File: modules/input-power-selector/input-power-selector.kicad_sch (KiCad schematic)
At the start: 33 parts, among them Q1 SI4909DY-T1-GE3, Q2 SI4909DY-T1-GE3, Q3 SI4909DY-T1-GE3, Q4 IPF067N20NM6ATMA1, Q5 BC547, Q6 SQJQ457EP, U1 LTC4417IGN

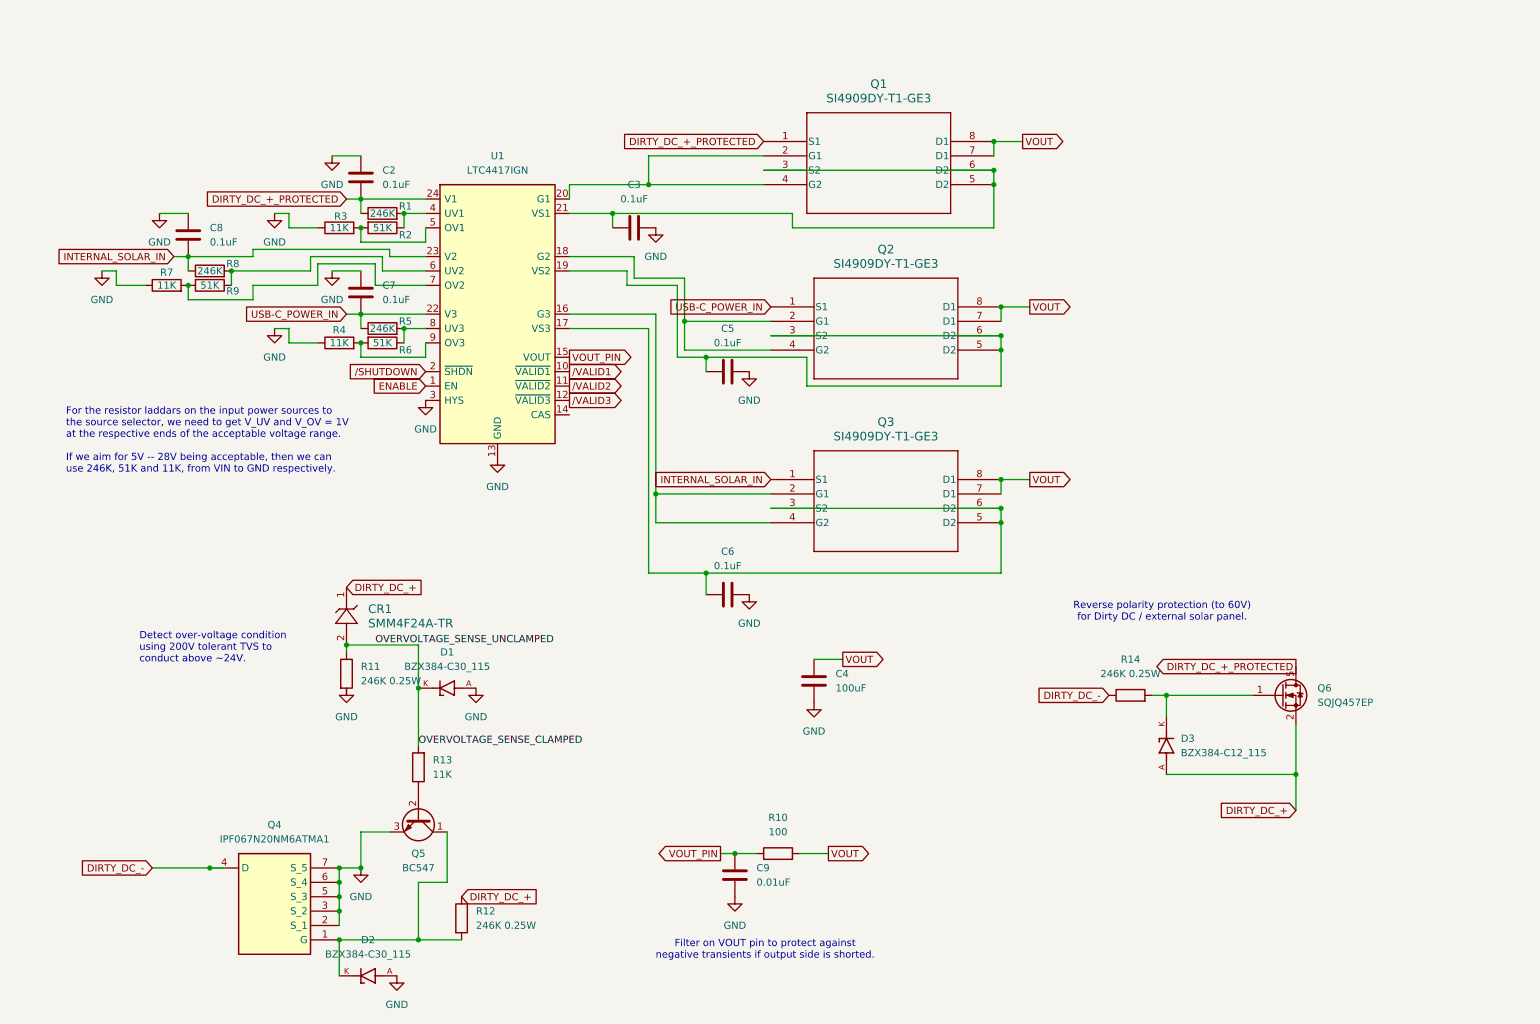
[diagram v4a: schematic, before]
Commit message: work on laying out power input selector
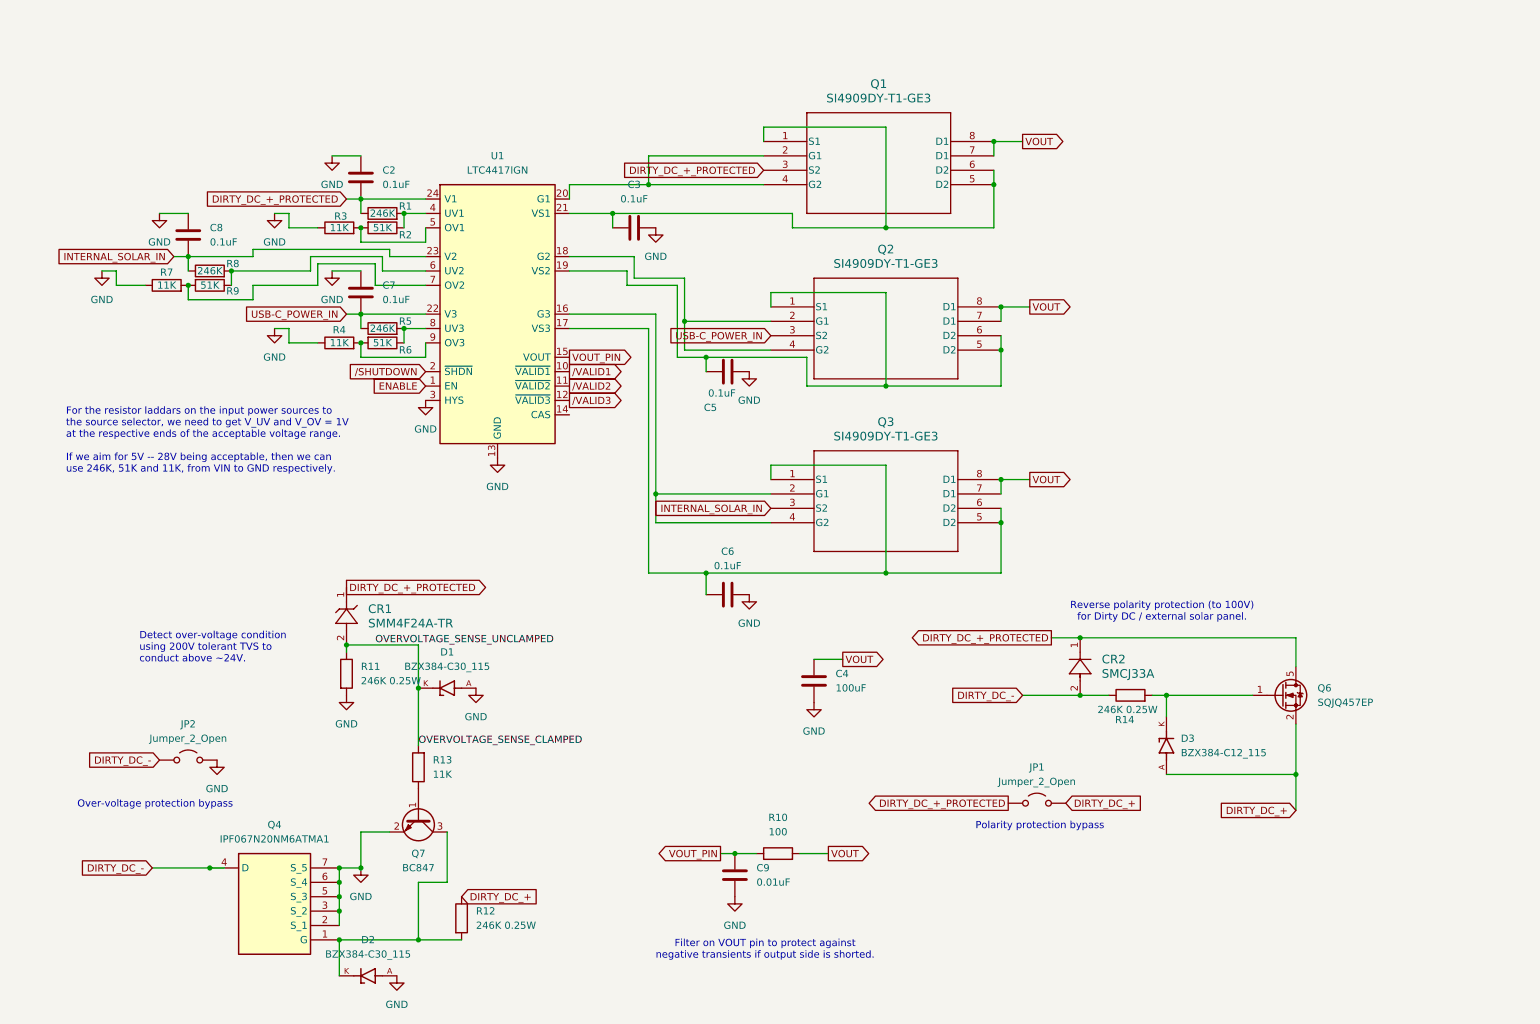
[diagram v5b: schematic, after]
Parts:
- removed Q5: BC547, Package_TO_SOT_THT:TO-92_Inline, symbol Transistor_BJT:BC547
- added CR2: SMCJ33A, DIODE_DO-214AC, symbol 2025-03-04_03-15-52:SMCJ28A
- added JP1, JP2: Jumper_2_Open, Jumper:SolderJumper-2_P1.3mm_Open_RoundedPad1.0x1.5mm, symbol Jumper:Jumper_2_Open
- added Q7: BC847, Package_TO_SOT_SMD:SOT-23, symbol Transistor_BJT:BC847
- C7: footprint (none) -> Capacitor_SMD:C_0805_2012Metric
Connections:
- net DIRTY_DC_+: now also JP1.2 (B); no longer CR1.1
- net DIRTY_DC_+_PROTECTED: now also CR1.1, Q1.3 (S2), CR2.1, JP1.1 (A); no longer Q1.1 (S1)
- net DIRTY_DC_-: now also CR2.2, JP2.1 (A)
- net GND: now also R11.2, JP2.2 (B), Q7.2 (E)
- net INTERNAL_SOLAR_IN: now also Q3.3 (S2); no longer Q3.1 (S1)
- net USB-C_POWER_IN: now also Q2.3 (S2); no longer Q2.1 (S1)
- net at D2.K, Q4.1 (G), R12.2: now also Q7.3 (C)
- net at C6.1, Q3.5 (D2), Q3.6 (D2)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: now also Q3.1 (S1); no longer Q3.3 (S2)
- net at R13.1: now also Q7.1 (B)
- net at C3.1, Q1.5 (D2), Q1.6 (D2)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: now also Q1.1 (S1); no longer Q1.3 (S2)
- net at C5.1, Q2.5 (D2), Q2.6 (D2)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: now also Q2.1 (S1); no longer Q2.3 (S2)
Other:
- note added: "Over-voltage protection bypass"
- note added: "Polarity protection bypass"
- note added: "Reverse polarity protection (to 100V) for Dirty DC / external solar panel."
- note removed: "Reverse polarity protection (to 60V) for Dirty DC / external solar panel."

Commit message: more layout fixing on power selector
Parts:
- D1, D2, D3: footprint BZX384-C30_115:DIO_BZX384-C30_115 -> footprints:DIO_BZX384-C30_115
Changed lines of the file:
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@@
 			)
 		)
-		(property "Footprint" "BZX384-C30_115:DIO_BZX384-C30_115"
+		(property "Footprint" "footprints:DIO_BZX384-C30_115"
 			(at 71.12 189.23 0)
 			(effects
@@
 			)
 		)
-		(property "Footprint" "BZX384-C30_115:DIO_BZX384-C30_115"
+		(property "Footprint" "footprints:DIO_BZX384-C30_115"
 			(at 85.09 138.43 0)
 			(effects
@@
 			)
 		)
-		(property "Footprint" "BZX384-C30_115:DIO_BZX384-C30_115"
+		(property "Footprint" "footprints:DIO_BZX384-C30_115"
 			(at 212.09 148.59 0)
 			(effects

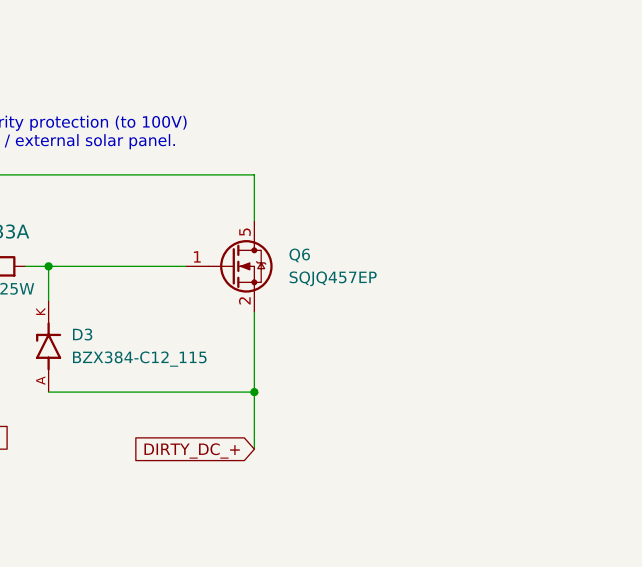
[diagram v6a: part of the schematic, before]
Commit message: update input source selecter PCB layout
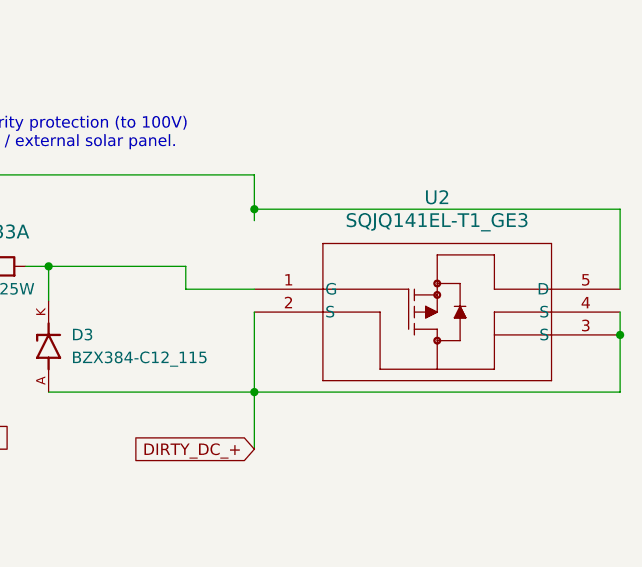
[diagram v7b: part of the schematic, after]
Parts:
- removed Q6: SQJQ457EP, Package_SO:PowerPAK_SO-8L_Single, symbol Transistor_FET:SQJQ466E
- added U2: SQJQ141EL-T1_GE3, PowerPAK_8x8L_BWL-2_VIS, symbol 2025-03-04_11-28-00:SQJQ141EL-T1_GE3
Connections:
- net DIRTY_DC_+: now also U2.2 (S), U2.3 (S), U2.4 (S)
- net DIRTY_DC_+_PROTECTED: now also U2.5 (D)
- net at D3.K, R14.2: now also U2.1 (G)
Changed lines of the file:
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@@
 	)
 	(junction
+		(at 234.95 133.35)
+		(diameter 0)
+		(color 0 0 0 0)
+	)
+	(junction
 		(at 196.85 129.54)
 		(diameter 0)
@@
 	)
 	(junction
+		(at 275.59 147.32)
+		(diameter 0)
+		(color 0 0 0 0)
+	)
+	(junction
 		(at 162.56 118.11)
 		(diameter 0)
@@
 	(wire
 		(pts
-			(xy 234.95 134.62) (xy 234.95 129.54)
+			(xy 39.37 62.23) (xy 39.37 64.77)
 		)
 		(stroke
@@
 	(wire
 		(pts
-			(xy 39.37 62.23) (xy 39.37 64.77)
+			(xy 73.66 62.23) (xy 73.66 64.77)
 		)
 		(stroke
@@
 	(wire
 		(pts
-			(xy 73.66 62.23) (xy 73.66 64.77)
+			(xy 39.37 62.23) (xy 50.8 62.23)
 		)
 		(stroke
@@
 	(wire
 		(pts
-			(xy 39.37 62.23) (xy 50.8 62.23)
+			(xy 130.81 80.01) (xy 130.81 82.55)
 		)
 		(stroke
@@
 	(wire
 		(pts
-			(xy 130.81 80.01) (xy 130.81 82.55)
+			(xy 125.73 67.31) (xy 125.73 80.01)
 		)
 		(stroke
@@
 	(wire
 		(pts
-			(xy 125.73 67.31) (xy 125.73 80.01)
+			(xy 106.68 49.53) (xy 120.65 49.53)
 		)
 		(stroke
@@
 	(wire
 		(pts
-			(xy 106.68 49.53) (xy 120.65 49.53)
+			(xy 80.01 138.43) (xy 80.01 130.81)
 		)
 		(stroke
@@
 	(wire
 		(pts
-			(xy 80.01 138.43) (xy 80.01 130.81)
+			(xy 234.95 129.54) (xy 234.95 133.35)
 		)
 		(stroke
@@
 	(wire
 		(pts
+			(xy 275.59 147.32) (xy 275.59 153.67)
+		)
+		(stroke
+			(width 0)
+			(type default)
+		)
+	)
+	(wire
+		(pts
 			(xy 72.39 63.5) (xy 62.23 63.5)
 		)
@@
 	(wire
 		(pts
+			(xy 234.95 133.35) (xy 234.95 134.62)
+		)
+		(stroke
+			(width 0)
+			(type default)
+		)
+	)
+	(wire
+		(pts
 			(xy 69.85 59.69) (xy 69.85 57.15)
 		)
@@
 	(wire
 		(pts
+			(xy 234.95 142.24) (xy 227.33 142.24)
+		)
+		(stroke
+			(width 0)
+			(type default)
+		)
+	)
+	(wire
+		(pts
 			(xy 120.65 49.53) (xy 140.97 49.53)
 		)
@@
 	(wire
 		(pts
+			(xy 275.59 144.78) (xy 275.59 147.32)
+		)
+		(stroke
+			(width 0)
+			(type default)
+		)
+	)
+	(wire
+		(pts
 			(xy 182.88 101.6) (xy 187.96 101.6)
 		)
@@
 	(wire
 		(pts
+			(xy 234.95 133.35) (xy 275.59 133.35)
+		)
+		(stroke
+			(width 0)
+			(type default)
+		)
+	)
+	(wire
+		(pts
 			(xy 118.11 66.04) (xy 127 66.04)
 		)
@@
 	(wire
 		(pts
+			(xy 227.33 142.24) (xy 227.33 139.7)
+		)
+		(stroke
+			(width 0)
+			(type default)
+		)
+	)
+	(wire
+		(pts
 			(xy 120.65 74.93) (xy 120.65 118.11)
 		)
@@
 	(wire
 		(pts
+			(xy 275.59 153.67) (xy 234.95 153.67)
+		)
+		(stroke
+			(width 0)
+			(type default)
+		)
+	)
+	(wire
+		(pts
 			(xy 182.88 109.22) (xy 182.88 118.11)
 		)
@@
 	(wire
 		(pts
+			(xy 275.59 133.35) (xy 275.59 142.24)
+		)
+		(stroke
+			(width 0)
+			(type default)
+		)
+	)
+	(wire
+		(pts
 			(xy 181.61 41.91) (xy 181.61 44.45)
 		)
@@
 	)
 	(symbol
+		(lib_id "2025-03-04_11-28-00:SQJQ141EL-T1_GE3")
+		(at 234.95 142.24 0)
+		(unit 1)
+		(exclude_from_sim no)
+		(in_bom yes)
+		(on_board yes)
+		(dnp no)
+		(fields_autoplaced yes)
+		(property "Reference" "U2"
+			(at 255.27 132.08 0)
+			(effects
+				(font
+					(size 1.524 1.524)
+				)
+			)
+		)
+		(property "Value" "SQJQ141EL-T1_GE3"
+			(at 255.27 134.62 0)
+			(effects
+				(font
+					(size 1.524 1.524)
+				)
+			)
+		)
+		(property "Footprint" "PowerPAK_8x8L_BWL-2_VIS"
+			(at 234.95 142.24 0)
+			(effects
+				(font
+					(size 1.27 1.27)
+					(italic yes)
+				)
+				(hide yes)
+			)
+		)
+		(property "Datasheet" "SQJQ141EL-T1_GE3"
+			(at 234.95 142.24 0)
+			(effects
+				(font
+					(size 1.27 1.27)
+					(italic yes)
+				)
+				(hide yes)
+			)
+		)
+		(property "Description" ""
+			(at 234.95 142.24 0)
+			(effects
+				(font
+					(size 1.27 1.27)
+				)
+				(hide yes)
+			)
+		)
+		(pin "2"
+		)
+		(pin "5"
+		)
+		(pin "4"
+		)
+		(pin "3"
+		)
+		(pin "1"
+		)
+		(instances
+			(project ""
+				(path "/c18eebf3-c622-42ce-a76a-45e5fabab2b4"
+					(reference "U2")
+					(unit 1)
+				)
+			)
+		)
+	)
+	(symbol
 		(lib_id "Device:R")
 		(at 73.66 57.15 270)
@@
 					(unit 1)
 				)
-			)
-		)
-	)
-	(symbol
-		(lib_id "Transistor_FET:SQJQ466E")
-		(at 232.41 139.7 0)
-		(unit 1)
-		(exclude_from_sim no)
-		(in_bom yes)
-		(on_board yes)
-		(dnp no)
-		(fields_autoplaced yes)
-		(property "Reference" "Q6"
-			(at 238.76 138.4299 0)
-			(effects
-				(font
-					(size 1.27 1.27)
-				)
-				(justify left)
-			)
-		)
-		(property "Value" "SQJQ457EP"
-			(at 238.76 140.9699 0)
-			(effects
-				(font
-					(size 1.27 1.27)
-				)
-				(justify left)
-			)
-		)
-		(property "Footprint" "Package_SO:PowerPAK_SO-8L_Single"
-			(at 237.49 143.51 0)
-			(effects
-				(font
-					(size 1.27 1.27)
-				)
-				(justify left)
-				(hide yes)
-			)
-		)
-		(property "Datasheet" "https://www.vishay.com/docs/75138/sqjq466e.pdf"
-			(at 237.49 146.05 0)
-			(effects
-				(font
-					(size 1.27 1.27)
-				)
-				(justify left)
-				(hide yes)
-			)
-		)
-		(property "Description" "200A Id, 60V Vds, N-Channel TrenchFET MOSFET, 1.9mOhm Ron, 14nC Qqd, -55 to 175 °C, LFPAK88"
-			(at 232.41 139.7 0)
-			(effects
-				(font
-					(size 1.27 1.27)
-				)
-				(hide yes)
-			)
-		)
-		(pin "1"
-		)
-		(pin "5"
-		)
-		(pin "4"
-		)
-		(pin "3"
-		)
-		(pin "2"
-		)
-		(instances
-			(project ""
-				(path "/c18eebf3-c622-42ce-a76a-45e5fabab2b4"
-					(reference "Q6")
-					(unit 1)
-				)

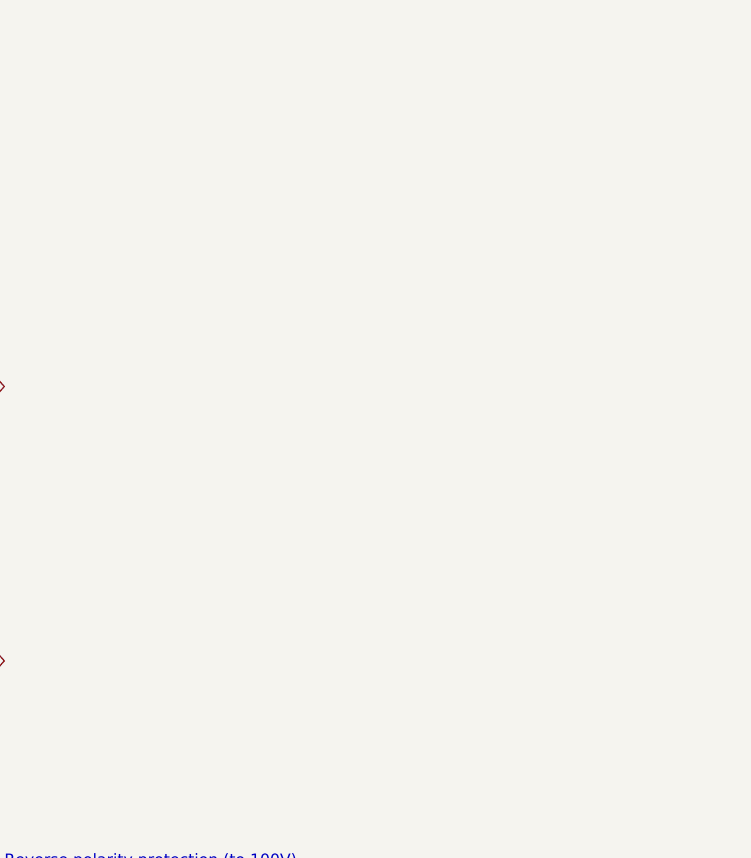
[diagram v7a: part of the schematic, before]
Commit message: add module outline for input source selecter
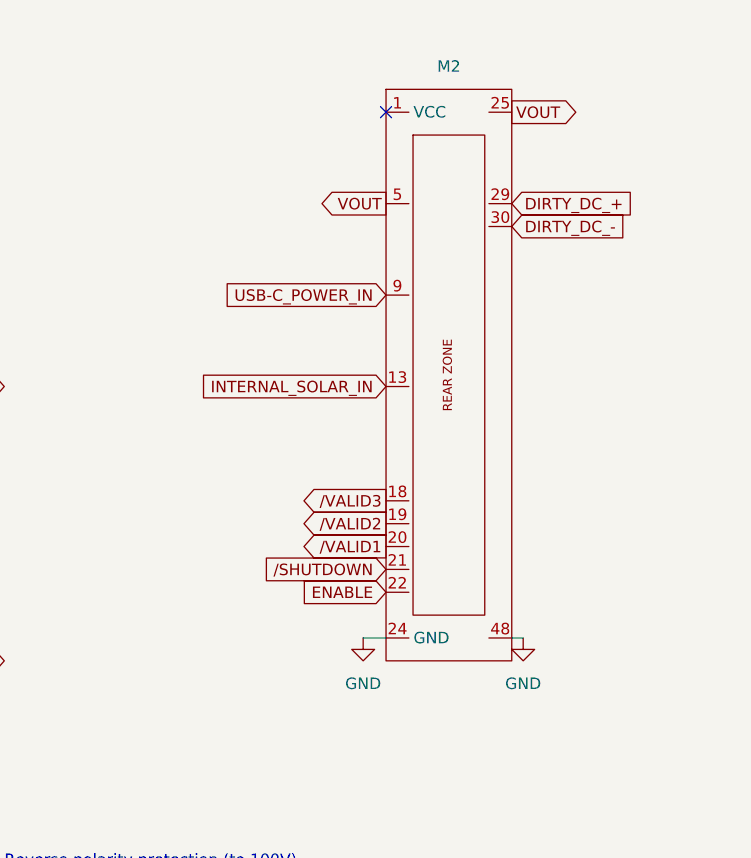
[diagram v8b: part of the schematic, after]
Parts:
- added M2: ~, MegaCastle:MegaCastle2x24-Module-I42.0x56.2-M88887D8C0001, symbol MegaCastle:MegaCastle2x24-Module-I42.0x56.2-M88887D8C0001
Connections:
- net DIRTY_DC_+: now also M2.29
- net DIRTY_DC_-: now also M2.30
- net ENABLE: now also M2.22
- net GND: now also M2.24 (GND), M2.48
- net INTERNAL_SOLAR_IN: now also M2.13
- net USB-C_POWER_IN: now also M2.9
- net VOUT: now also M2.25, M2.5
- net /SHUTDOWN: now also M2.21
- net /VALID1: now also M2.20
- net /VALID2: now also M2.19
- net /VALID3: now also M2.18
- no-connect marks 0 -> 1
